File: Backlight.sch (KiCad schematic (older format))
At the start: 15 parts, among them P3 4pin_Joint_Tech_0_5mm, U1 LM27313

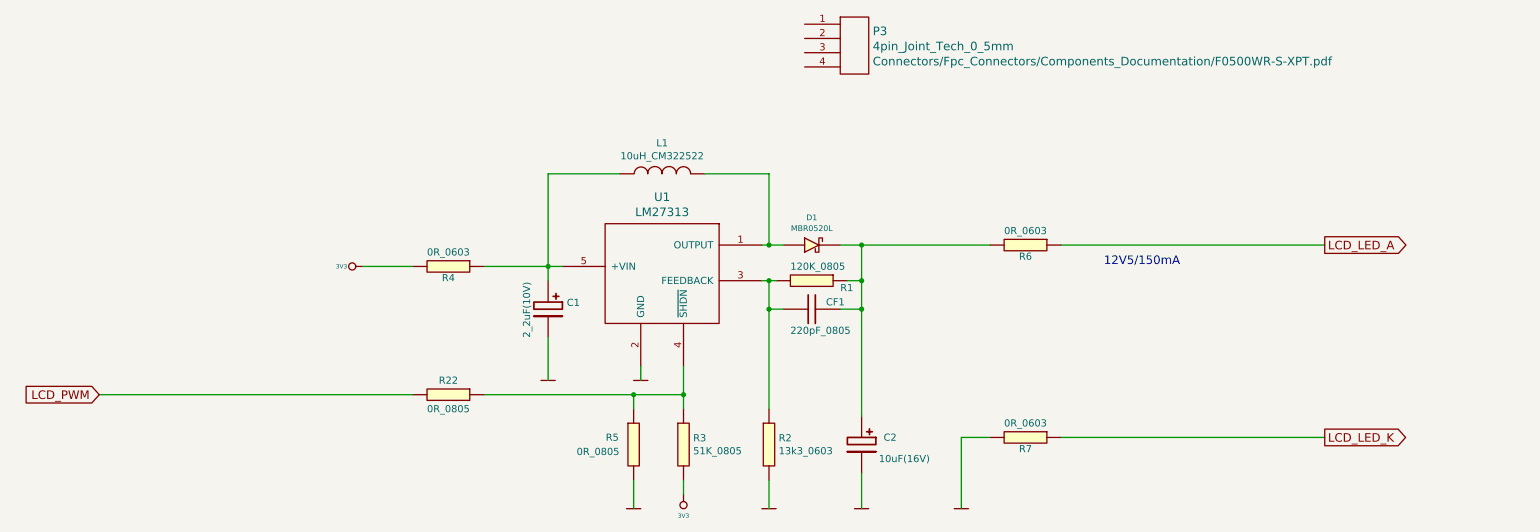
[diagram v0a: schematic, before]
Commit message: Schematic finished, needes to be rechecked, pcb finished needes to be tweeked
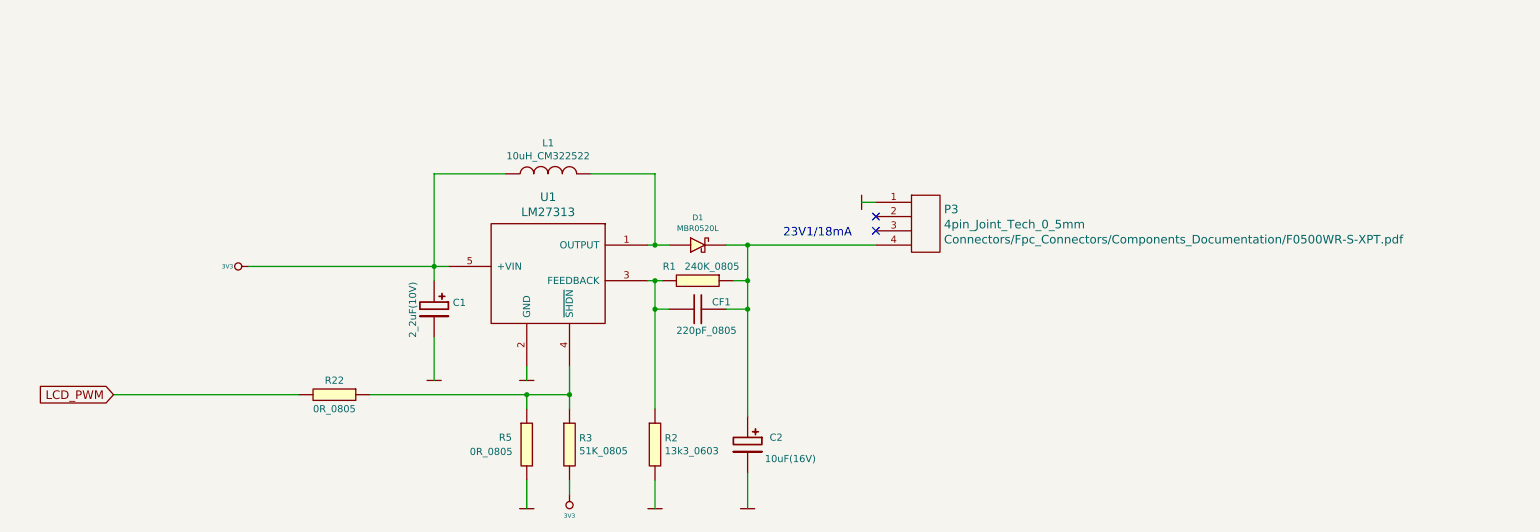
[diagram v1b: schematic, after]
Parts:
- removed R1: 120K_0805, Resistor_Smd_0805:120k_0805, symbol 120K_0805
- removed R4, R6, R7: 0R_0603, Resistor_Smd_0603:0R_0603, symbol 0R_0603
- added R1: 240K_0805, Resistor_Smd_0805:240k_0805, symbol 240K_0805
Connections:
- net 3V3: now also C1.1, L1.1, U1.5 (+VIN)
- net GND: now also P3.1 (P1)
- net at C2.1, CF1.1, D1.1 (K): now also P3.4 (P4), R1.1
- net at CF1.2, R2.1, U1.3 (FEEDBACK): now also R1.2
- no-connect marks 0 -> 2
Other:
- note added: "23V1/18mA"
- note removed: "12V5/150mA"
- moved on the sheet: C1, C2, CF1, D1, L1, P3, R2, R22, R3, R5, U1

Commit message: Corrected FPC 40pin top 0.5mm connector, generated again gerber and ps files
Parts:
- C1: symbol 2_2uF_10V_SMD_Tantal -> Capacitors_Smd_Tantal:2_2uF_10V_SMD_Tantal
- C2: symbol 10uF_16V_SMD_Tantal -> Capacitors_Smd_Tantal:10uF_16V_SMD_Tantal
- CF1: symbol 220pF_0805 -> Capacitors_Smd0805:220pF_0805
- D1: symbol MBR0520L -> Diodes:MBR0520L
- L1: symbol 10uH_CM322522 -> Inductors:10uH_CM322522
- P3: symbol 4pin_Joint_Tech_0_5mm -> Fpc_Connectors:4pin_Joint_Tech_0_5mm
- R1: symbol 240K_0805 -> Resistors_Smd0805:240K_0805
- R2: symbol 13k3_0603 -> Resistors_Smd0603:13k3_0603
- R22, R5: symbol 0R_0805 -> Resistors_Smd0805:0R_0805
- R3: symbol 51K_0805 -> Resistors_Smd0805:51K_0805
- U1: symbol LM27313 -> Switching_Regulators:LM27313
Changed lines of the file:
@@
-EESchema Schematic File Version 3
-LIBS:Capacitors_Smd0805
-LIBS:Capacitors_Smd_Tantal
-LIBS:Fpc_Connectors
-LIBS:Switching_Regulators
-LIBS:Diodes
-LIBS:Inductors
-LIBS:power
-LIBS:Resistors_Smd0603
-LIBS:Resistors_Smd0805
-LIBS:Symbols
-LIBS:Touch_Sensors
+EESchema Schematic File Version 4
 LIBS:TFT_LCD_4_3_AM480272H2T_V1_0-cache
 EELAYER 26 0
@@
 $EndDescr
 $Comp
-L 2_2uF_10V_SMD_Tantal C1
+L Capacitors_Smd_Tantal:2_2uF_10V_SMD_Tantal C1
 U 1 1 578A98DF
 P 3900 3700
@@
 $EndComp
 $Comp
-L 220pF_0805 CF1
+L Capacitors_Smd0805:220pF_0805 CF1
 U 1 1 578A992D
 P 5750 3750
@@
 $EndComp
 $Comp
-L 10uH_CM322522 L1
+L Inductors:10uH_CM322522 L1
 U 1 1 578A9965
 P 4700 2800
@@
 $EndComp
 $Comp
-L 51K_0805 R3
+L Resistors_Smd0805:51K_0805 R3
 U 1 1 578A9A11
 P 4850 4700
@@
 $EndComp
 $Comp
-L 13k3_0603 R2
+L Resistors_Smd0603:13k3_0603 R2
 U 1 1 578A9A5B
 P 5450 4700
@@
 	4850 4150 4850 4450
 $Comp
-L GND #PWR08
+L power1:GND #PWR08
 U 1 1 578AA0D3
 P 4550 4250
@@
 	4850 4950 4850 5050
 $Comp
-L GND #PWR09
+L power1:GND #PWR09
 U 1 1 578AA46D
 P 3900 4250
@@
 	3900 3950 3900 4250
 $Comp
-L LM27313 U1
+L Switching_Regulators:LM27313 U1
 U 1 1 578AAA95
 P 4700 3500
@@
 Connection ~ 6100 3300
 $Comp
-L MBR0520L D1
+L Diodes:MBR0520L D1
 U 1 1 578A99B5
 P 5750 3300
@@
 Connection ~ 5450 3550
 $Comp
-L GND #PWR010
+L power1:GND #PWR010
 U 1 1 578AB087
 P 5450 5150
@@
 Connection ~ 6100 3550
 $Comp
-L GND #PWR011
+L power1:GND #PWR011
 U 1 1 578AB379
 P 6100 5150
@@
 	2600 3450 4000 3450
 $Comp
-L 3V3 #PWR012
+L power1:3V3 #PWR012
 U 1 1 57E9AAD9
 P 2600 3450
@@
 $EndComp
 $Comp
-L 0R_0805 R5
+L Resistors_Smd0805:0R_0805 R5
 U 1 1 57E9ACB8
 P 4550 4700
@@
 $EndComp
 $Comp
-L GND #PWR013
+L power1:GND #PWR013
 U 1 1 57E9AD53
 P 4550 5150
@@
 	3450 4350 4850 4350
 $Comp
-L GND #PWR014
+L power1:GND #PWR014
 U 1 1 57E9B3F0
 P 6900 3000
@@
 $EndComp
 $Comp
-L 3V3 #PWR015
+L power1:3V3 #PWR015
 U 1 1 57ECB801
 P 4850 5050
@@
 $EndComp
 $Comp
-L 10uF_16V_SMD_Tantal C2
+L Capacitors_Smd_Tantal:10uF_16V_SMD_Tantal C2
 U 1 1 57EECEF5
 P 6100 4650
@@
 $EndComp
 $Comp
-L 0R_0805 R22
+L Resistors_Smd0805:0R_0805 R22
 U 1 1 59E857B6
 P 3200 4350
@@
 	2950 4350 1650 4350
 $Comp
-L 4pin_Joint_Tech_0_5mm P3
+L Fpc_Connectors:4pin_Joint_Tech_0_5mm P3
 U 1 1 59F3C6E8
 P 7250 3150
@@
 NoConn ~ 7000 3200
 $Comp
-L 240K_0805 R1
+L Resistors_Smd0805:240K_0805 R1
 U 1 1 59F4EE54
 P 5750 3550
